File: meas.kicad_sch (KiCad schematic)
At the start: 13 parts, among them J101 Conn_01x06_Socket, J102 Conn_01x02_Socket, J103 Conn_01x02_Socket, J104 Conn_01x02_Socket, J105 Conn_01x02_Socket

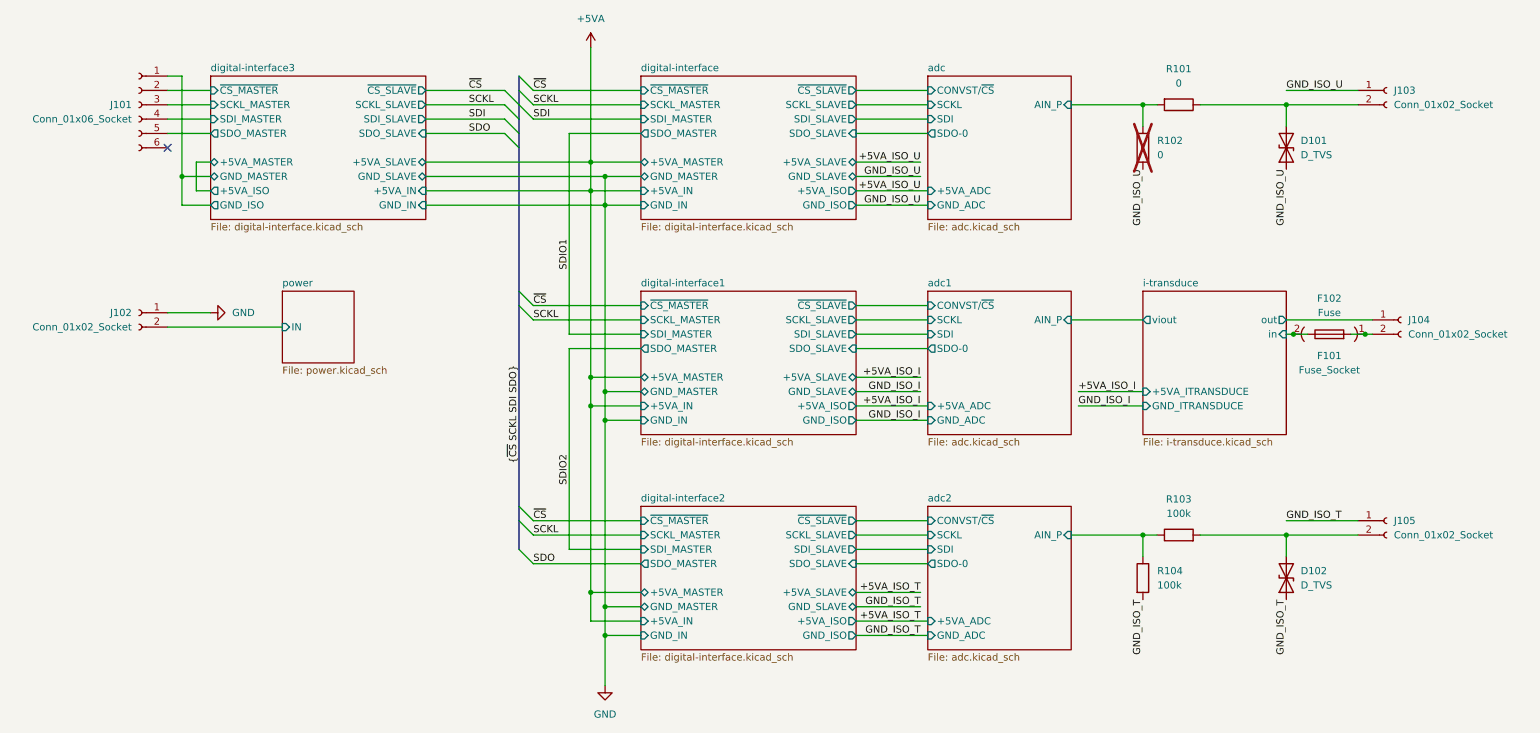
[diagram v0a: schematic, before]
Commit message: separate digital-interface and iso-dcdc
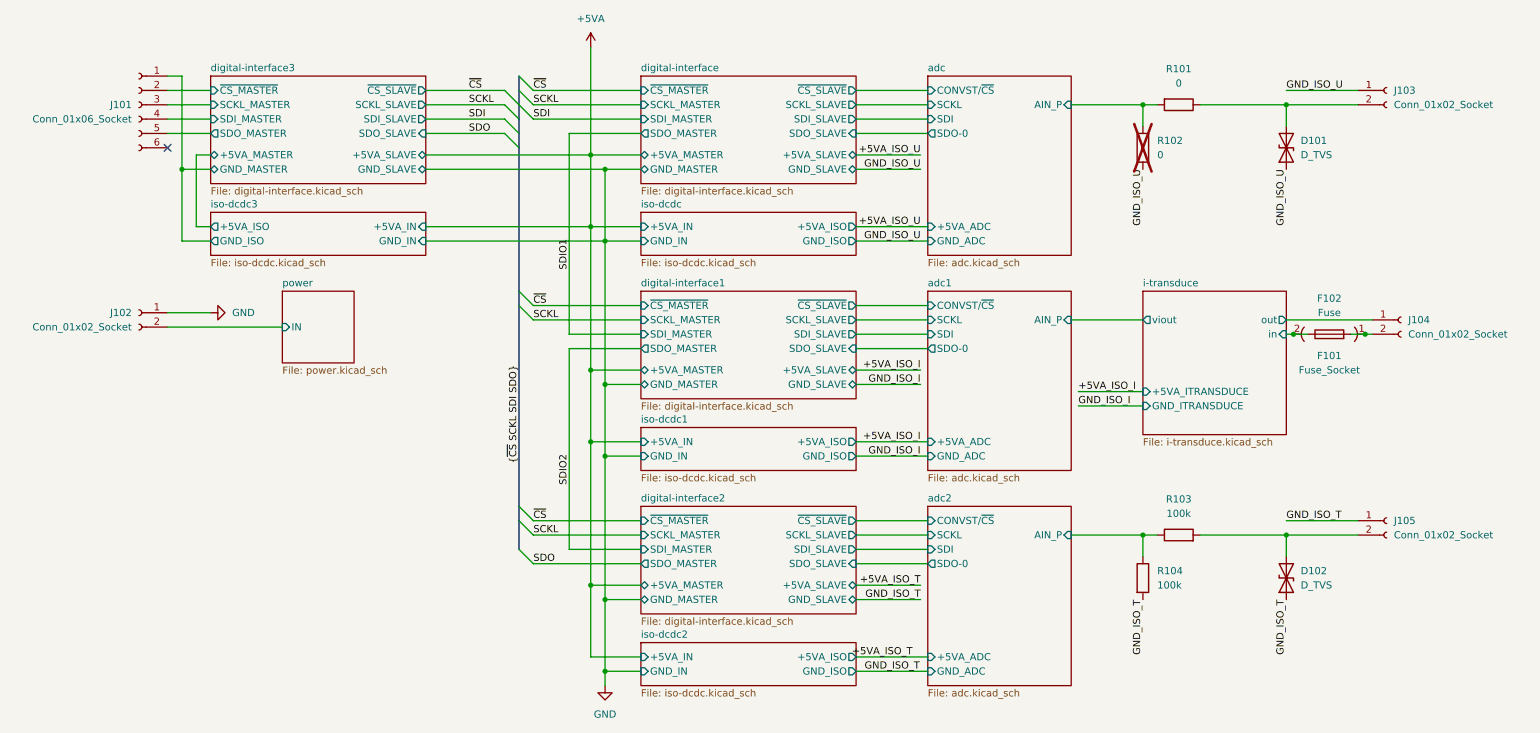
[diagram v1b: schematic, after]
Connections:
- net digital-interface3/GND_ISO renamed digital-interface3/GND_MASTER
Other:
- added sheet iso-dcdc (iso-dcdc.kicad_sch)
- added sheet iso-dcdc1 (iso-dcdc.kicad_sch)
- added sheet iso-dcdc2 (iso-dcdc.kicad_sch)
- added sheet iso-dcdc3 (iso-dcdc.kicad_sch)
- sheet digital-interface ports: added none; removed +5VA_IN, +5VA_ISO, GND_IN, GND_ISO
- sheet digital-interface1 ports: added none; removed +5VA_IN, +5VA_ISO, GND_IN, GND_ISO
- sheet digital-interface2 ports: added none; removed +5VA_IN, +5VA_ISO, GND_IN, GND_ISO
- sheet digital-interface3 ports: added none; removed +5VA_IN, +5VA_ISO, GND_IN, GND_ISO

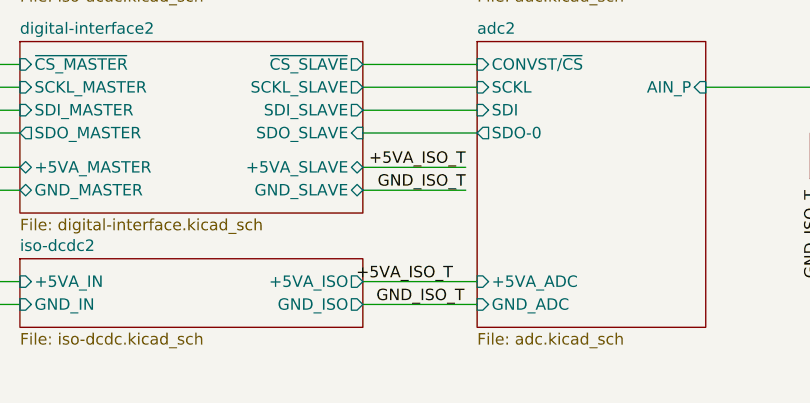
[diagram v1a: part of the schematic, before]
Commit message: resize pcb to 100x130 mm^2
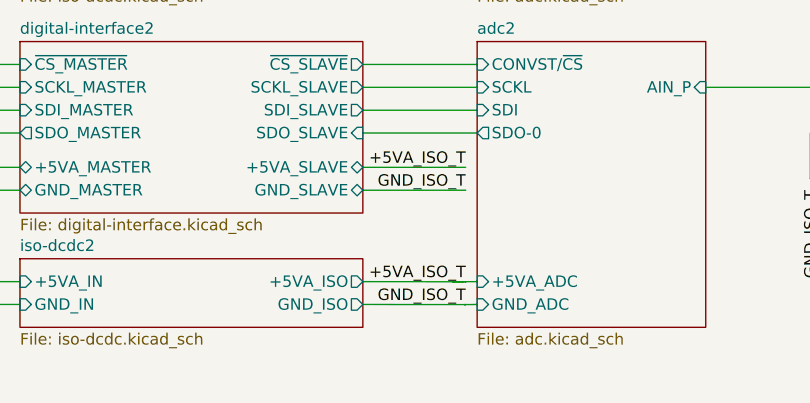
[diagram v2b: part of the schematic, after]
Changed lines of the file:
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@@
+	(wire
+		(pts
+			(xy 176.53 140.97) (xy 176.53 140.9895)
+		)
+		(stroke
+			(width 0)
+			(type default)
+		)
+	)
 	(wire
 		(pts
@@
 	(wire
 		(pts
+			(xy 176.53 140.9895) (xy 175.1037 140.9895)
+		)
+		(stroke
+			(width 0)
+			(type default)
+		)
+	)
+	(wire
+		(pts
 			(xy 165.1 54.61) (xy 176.53 54.61)
 		)
@@
 	(wire
 		(pts
+			(xy 176.53 143.5255) (xy 176.3906 143.5255)
+		)
+		(stroke
+			(width 0)
+			(type default)
+		)
+	)
+	(wire
+		(pts
 			(xy 88.9 64.77) (xy 118.11 64.77)
 		)
@@
 	(wire
 		(pts
+			(xy 176.53 143.51) (xy 176.53 143.5255)
+		)
+		(stroke
+			(width 0)
+			(type default)
+		)
+	)
+	(wire
+		(pts
 			(xy 241.3 40.64) (xy 254 40.64)
 		)
@@
 	(wire
 		(pts
-			(xy 165.1 140.97) (xy 177.8 140.97)
+			(xy 165.1 140.97) (xy 175.1037 140.9895)
 		)
 		(stroke
@@
 	(wire
 		(pts
+			(xy 175.1037 140.9895) (xy 177.8 140.97)
+		)
+		(stroke
+			(width 0)
+			(type default)
+		)
+	)
+	(wire
+		(pts
 			(xy 120.65 105.41) (xy 120.65 130.81)
 		)
@@
 	(wire
 		(pts
-			(xy 165.1 143.51) (xy 177.8 143.51)
+			(xy 165.1 143.51) (xy 176.3906 143.5255)
 		)
 		(stroke
@@
 		(pts
 			(xy 165.1 43.18) (xy 177.8 43.18)
+		)
+		(stroke
+			(width 0)
+			(type default)
+		)
+	)
+	(wire
+		(pts
+			(xy 176.3906 143.5255) (xy 177.8 143.51)
 		)
 		(stroke
@@
 	)
 	(label "GND_ISO_T"
-		(at 176.3906 143.5255 180)
+		(at 176.53 143.51 180)
 		(fields_autoplaced yes)
 		(effects
@@
 	)
 	(label "+5VA_ISO_T"
-		(at 175.1037 140.9895 180)
-		(fields_autoplaced yes)
-		(effects
+		(at 176.53 140.97 180)
+		(fields_autoplaced yes)
+		(effects
